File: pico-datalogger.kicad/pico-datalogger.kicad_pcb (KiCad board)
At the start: 2 copper layers, 81.6 x 90 mm, 37 parts, among them J1 JST-PH2 VCC, J10 Conn_Inky_SW, J11 I2C_1, J12 I2C_7, J14 I2C_6, J16 BG_2, J18 I2C_5, J19 I2C_4, J2 I2C_8, J20 BG_3, J21 Conn_GND, J3 RFM9x_Lora_Breakout, J4 Alt-VCC, J5 Conn_I2S, J6 Conn_Inky_SPI, J7 Micro_SD_TF_PUSH, J8 Conn_ADC, J9 Conn_UART, SW1 SW_Push_SLIM, SW2 SW_Reset, U1 SN74HC74N, U2 PCF8523T, U3 Pico, Y1 Crystal

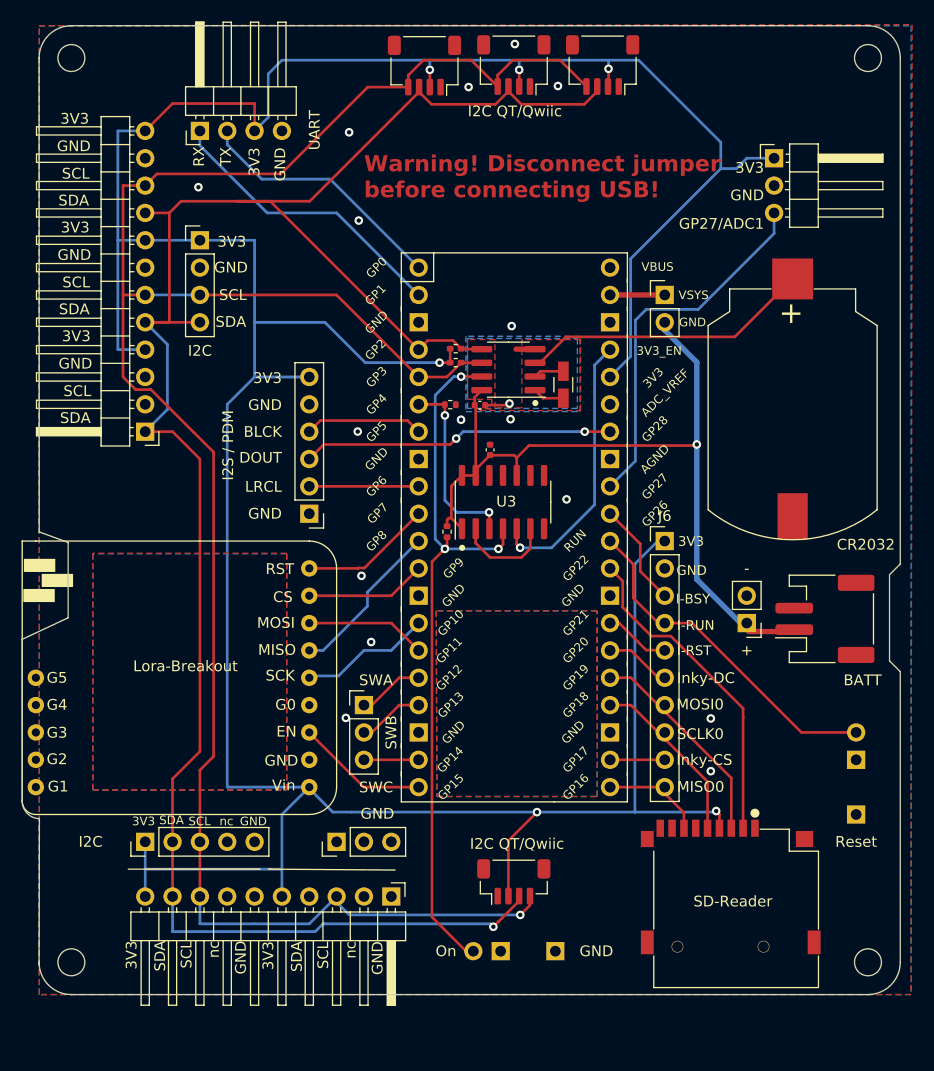
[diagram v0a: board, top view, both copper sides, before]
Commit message: Adjusted layout to 10th inch
No significant changes, bar moving inky switch pads. This layout has errors and warnings, esp "d thermal relief connection to zone incomplete".
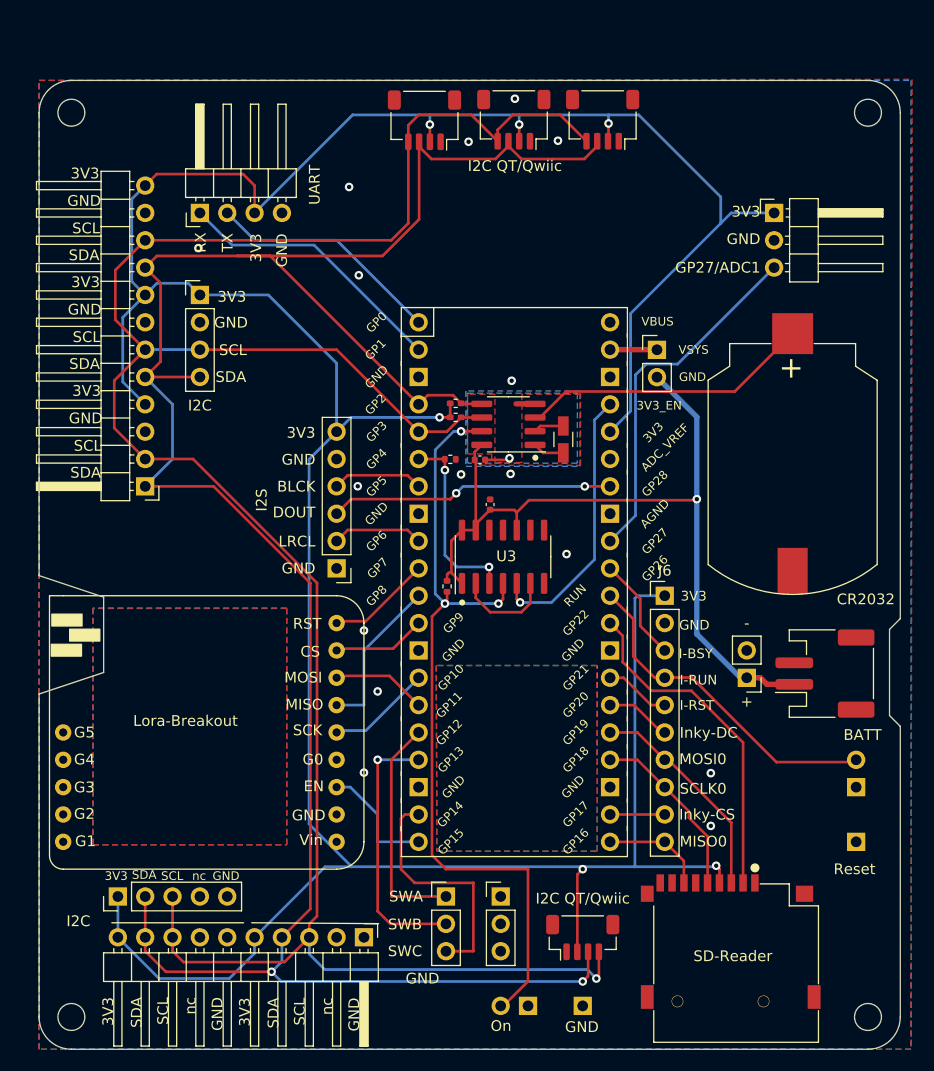
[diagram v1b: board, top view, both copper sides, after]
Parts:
- moved J10 19.3 mm to (129.5, 129.5)
- moved J21 16.1 mm to (134.6, 129.5), turned to 0 degrees
- moved J18 8.23 mm to (142.2, 133.3)
- moved J9 7.62 mm to (106.7, 66.0)
- moved J16 5.68 mm to (99.1, 129.5)
- moved J3 5.68 mm to (119.4, 124.5)
- moved J5 5.68 mm to (119.4, 99.1)
- moved SW1 5.68 mm to (142.2, 139.7)
- moved JP1 5.15 mm to (149.1, 78.8)
- moved J7 5.08 mm to (156.0, 133.6)
- moved R1 5.08 mm to (129.9, 88.9)
- moved U2 5.08 mm to (135.3, 85.7)
- moved J14 5.08 mm to (144.1, 57.4)
- moved J2 5.08 mm to (135.8, 57.4)
- moved J8 5.08 mm to (160.0, 66.0)
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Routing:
- net /SDA: track 193.8 -> 218.2 mm, vias 1 -> 2
- net /SCL: track 197.1 -> 219.6 mm
- net +3V3: track 333.2 -> 312.5 mm
- net /Inky_SWB: track 6.13 -> 24.7 mm, vias 0 -> 1
- net /Inky_SWC: track 5.08 -> 22.6 mm
- net /Inky_SWA: track 6.13 -> 21.4 mm
- net /1~{PRE}: track 67.7 -> 75.4 mm
- net /DOUT: track 29.0 -> 26.5 mm
- net /BLCK: track 11.0 -> 8.47 mm
- net /Lora_RST: track 12.3 -> 9.92 mm
- net /SCLK1: track 12.3 -> 9.92 mm
- net /Lora_CS: track 11.2 -> 8.87 mm
- net /MOSI1: track 11.2 -> 9.01 mm
- net /RX: track 27.4 -> 25.6 mm
- net /TX: track 23.8 -> 22.0 mm
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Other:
- board size 81.6 x 90 mm -> 80 x 90 mm
- board text added: "I2S"
- board text added: "https://github.com/bablokb/pcb-pico-datalogger https://opendeved.net/ilce Rev 1.01"
- board text removed: "I2S / PDM"
- board text removed: "Warning! Disconnect jumper before connecting USB!"
- board text removed: "https://github.com/bablokb/pcb-pico-datalogger https://opendeved.net/ilce Rev 1.00"
